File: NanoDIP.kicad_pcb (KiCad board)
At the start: 2 copper layers, 71.1 x 23.9 mm, 13 parts, among them SW1 SW_Push, U1 LM7805_TO220, U2 ATMEGA328P-PU, Y1 16 MHz

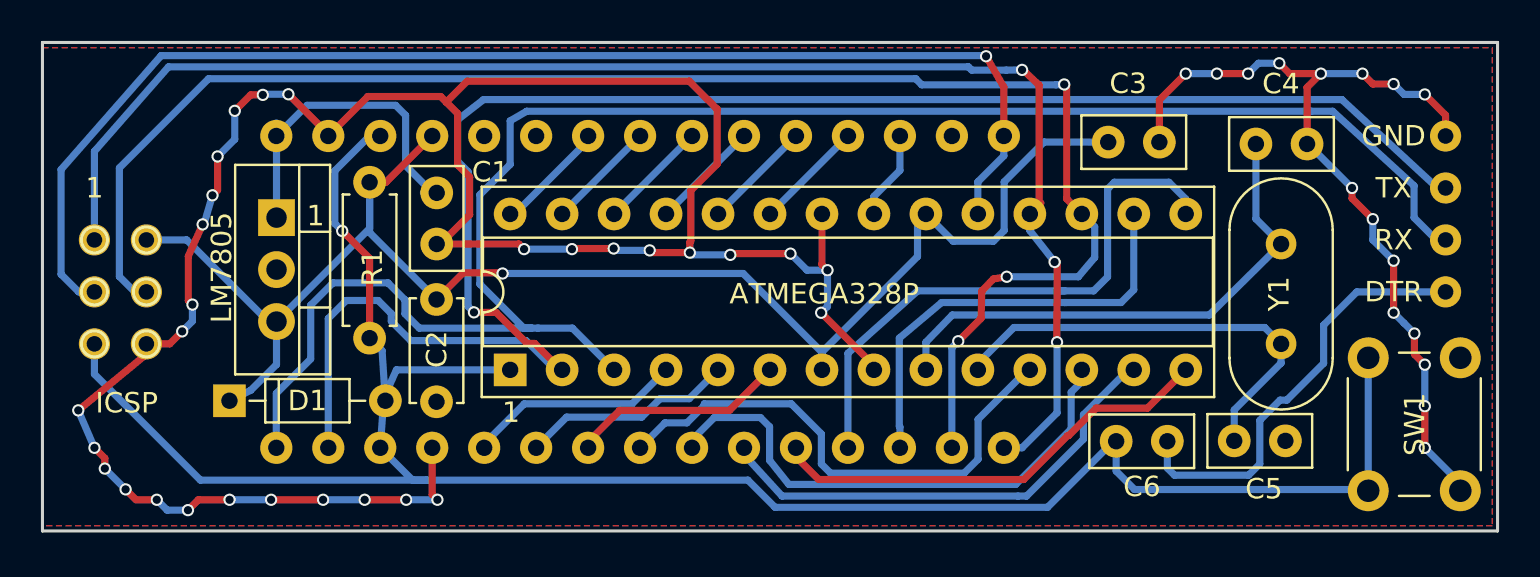
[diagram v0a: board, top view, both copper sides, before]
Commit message: Added pin labels
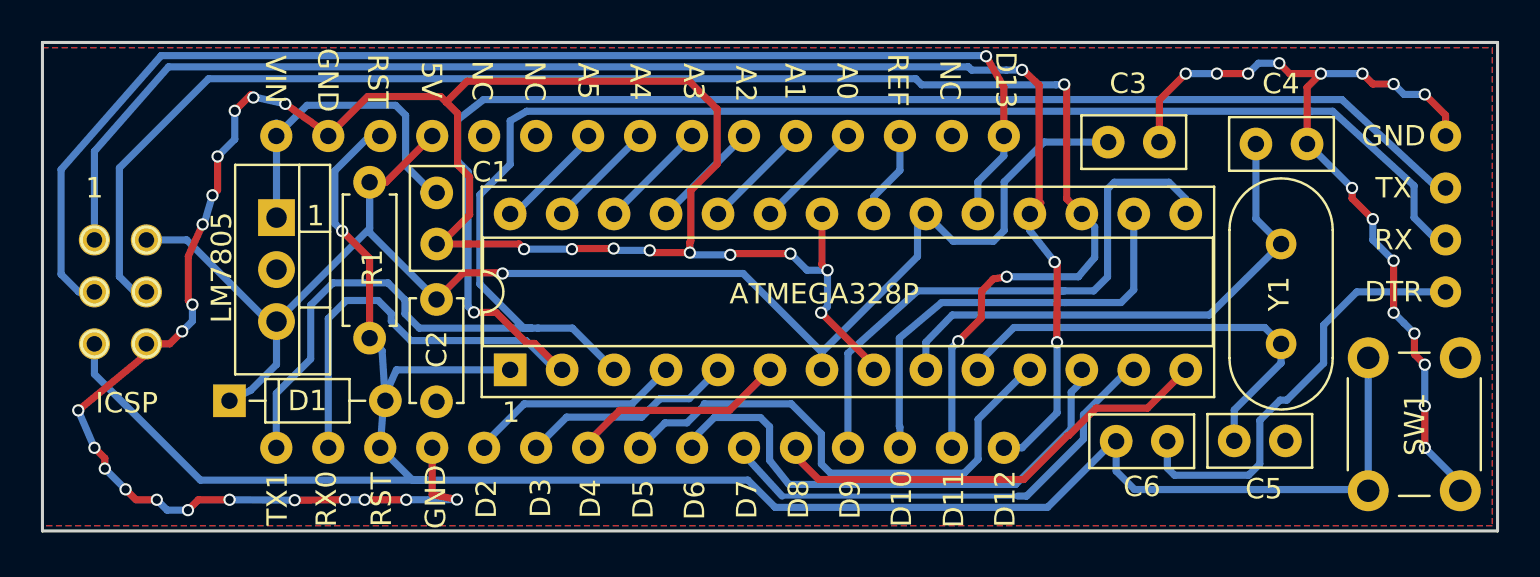
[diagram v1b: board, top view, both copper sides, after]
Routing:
- net GND: track 155.5 -> 157.1 mm
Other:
- board text added: "5V"
- board text added: "A0"
- board text added: "A1"
- board text added: "A2"
- board text added: "A3"
- board text added: "A4"
- board text added: "A5"
- board text added: "D10"
- board text added: "D11"
- board text added: "D12"
- board text added: "D13"
- board text added: "D2"
- board text added: "D3"
- board text added: "D4"
- board text added: "D5"
- board text added: "D6"
- board text added: "D7"
- board text added: "D8"
- board text added: "D9"
- board text added: "NC"
- board text added: "REF"
- board text added: "RST"
- board text added: "RX0"
- board text added: "TX1"
- board text added: "VIN"
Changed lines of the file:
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@@
     (links 62)
     (no_connects 0)
-    (area 121.844999 76.581999 193.115001 100.659001)
+    (area 121.844999 76.632999 193.115001 100.659001)
     (thickness 1.6)
-    (drawings 13)
+    (drawings 43)
     (tracks 443)
     (zones 0)
@@
   )
   (setup
-    (last_trace_width 0.35)
+    (last_trace_width 0.25)
     (user_trace_width 0.35)
     (trace_clearance 0.2)
@@
     (pad_to_mask_clearance 0.2)
     (aux_axis_origin 0 0)
-    (visible_elements FFFFFF7F)
+    (visible_elements 7FFFFFFF)
     (pcbplotparams
       (layerselection 0x00030_80000001)
@@
       (net 28 "Net-(A1-Pad40)"))
   )
+  (gr_text VIN (at 133.3 78.51 270) (layer F.SilkS)
+    (effects (font (size 1 1) (thickness 0.15)))
+  )
+  (gr_text GND (at 135.86 78.55 270) (layer F.SilkS)
+    (effects (font (size 1 1) (thickness 0.15)))
+  )
+  (gr_text RST (at 138.3 78.6 270) (layer F.SilkS)
+    (effects (font (size 1 1) (thickness 0.15)))
+  )
+  (gr_text 5V (at 140.93 78.54 270) (layer F.SilkS)
+    (effects (font (size 1 1) (thickness 0.15)))
+  )
+  (gr_text NC (at 143.4 78.57 270) (layer F.SilkS)
+    (effects (font (size 1 1) (thickness 0.15)))
+  )
+  (gr_text NC (at 145.98 78.6 270) (layer F.SilkS)
+    (effects (font (size 1 1) (thickness 0.15)))
+  )
+  (gr_text A5 (at 148.58 78.59 270) (layer F.SilkS)
+    (effects (font (size 1 1) (thickness 0.15)))
+  )
+  (gr_text A4 (at 151.12 78.64 270) (layer F.SilkS)
+    (effects (font (size 1 1) (thickness 0.15)))
+  )
+  (gr_text A3 (at 153.74 78.62 270) (layer F.SilkS)
+    (effects (font (size 1 1) (thickness 0.15)))
+  )
+  (gr_text A2 (at 156.29 78.73 270) (layer F.SilkS)
+    (effects (font (size 1 1) (thickness 0.15)))
+  )
+  (gr_text A1 (at 158.69 78.62 270) (layer F.SilkS)
+    (effects (font (size 1 1) (thickness 0.15)))
+  )
+  (gr_text A0 (at 161.24 78.61 270) (layer F.SilkS)
+    (effects (font (size 1 1) (thickness 0.15)))
+  )
+  (gr_text REF (at 163.72 78.55 270) (layer F.SilkS)
+    (effects (font (size 1 1) (thickness 0.15)))
+  )
+  (gr_text NC (at 166.27 78.55 270) (layer F.SilkS)
+    (effects (font (size 1 1) (thickness 0.15)))
+  )
+  (gr_text D13 (at 169 78.54 270) (layer F.SilkS)
+    (effects (font (size 1 1) (thickness 0.15)))
+  )
+  (gr_text D12 (at 168.97 99.01 90) (layer F.SilkS)
+    (effects (font (size 1 1) (thickness 0.15)))
+  )
+  (gr_text D11 (at 166.46 99.04 90) (layer F.SilkS)
+    (effects (font (size 1 1) (thickness 0.15)))
+  )
+  (gr_text D10 (at 163.91 99 90) (layer F.SilkS)
+    (effects (font (size 1 1) (thickness 0.15)))
+  )
+  (gr_text D9 (at 161.4 99.05 90) (layer F.SilkS)
+    (effects (font (size 1 1) (thickness 0.15)))
+  )
+  (gr_text D8 (at 158.88 99.04 90) (layer F.SilkS)
+    (effects (font (size 1 1) (thickness 0.15)))
+  )
+  (gr_text D7 (at 156.35 99.04 90) (layer F.SilkS)
+    (effects (font (size 1 1) (thickness 0.15)))
+  )
+  (gr_text D6 (at 153.8 99.09 90) (layer F.SilkS)
+    (effects (font (size 1 1) (thickness 0.15)))
+  )
+  (gr_text D5 (at 151.28 99.04 90) (layer F.SilkS)
+    (effects (font (size 1 1) (thickness 0.15)))
+  )
+  (gr_text D4 (at 148.71 99.01 90) (layer F.SilkS)
+    (effects (font (size 1 1) (thickness 0.15)))
+  )
+  (gr_text D3 (at 146.27 98.97 90) (layer F.SilkS)
+    (effects (font (size 1 1) (thickness 0.15)))
+  )
+  (gr_text D2 (at 143.62 99.02 90) (layer F.SilkS)
+    (effects (font (size 1 1) (thickness 0.15)))
+  )
+  (gr_text GND (at 141.14 98.92 90) (layer F.SilkS)
+    (effects (font (size 1 1) (thickness 0.15)))
+  )
+  (gr_text RX0 (at 135.8 99.02 90) (layer F.SilkS)
+    (effects (font (size 1 1) (thickness 0.15)))
+  )
+  (gr_text RST (at 138.49 99.05 90) (layer F.SilkS)
+    (effects (font (size 1 1) (thickness 0.15)))
+  )
+  (gr_text TX1 (at 133.4 99 90) (layer F.SilkS)
+    (effects (font (size 1 1) (thickness 0.15)))
+  )
   (gr_text LM7805 (at 130.68 87.71 90) (layer F.SilkS)
     (effects (font (size 1 1) (thickness 0.15)))
@@
   (segment (start 141.38 79.35) (end 137.82 79.35) (width 0.35) (layer F.Cu) (net 3))
   (segment (start 127 91.44) (end 128.14 91.44) (width 0.35) (layer F.Cu) (net 3))
-  (segment (start 133.94 79.24) (end 135.89 81.19) (width 0.35) (layer F.Cu) (net 3))
-  (via (at 133.94 79.24) (size 0.6) (drill 0.4) (layers F.Cu B.Cu) (net 3))
-  (segment (start 132.72 79.24) (end 133.94 79.24) (width 0.35) (layer B.Cu) (net 3))
-  (segment (start 132.69 79.27) (end 132.72 79.24) (width 0.35) (layer B.Cu) (net 3))
-  (via (at 132.69 79.27) (size 0.6) (drill 0.4) (layers F.Cu B.Cu) (net 3))
-  (segment (start 132.1 79.27) (end 132.69 79.27) (width 0.35) (layer F.Cu) (net 3))
+  (segment (start 133.79 79.71) (end 135.89 81.19) (width 0.35) (layer F.Cu) (net 3))
+  (via (at 133.79 79.71) (size 0.6) (drill 0.4) (layers F.Cu B.Cu) (net 3))
+  (segment (start 132.26 79.37) (end 133.79 79.71) (width 0.35) (layer B.Cu) (net 3))
+  (segment (start 132.23 79.4) (end 132.26 79.37) (width 0.35) (layer B.Cu) (net 3))
+  (via (at 132.23 79.4) (size 0.6) (drill 0.4) (layers F.Cu B.Cu) (net 3))
+  (segment (start 132.1 79.27) (end 132.23 79.4) (width 0.35) (layer F.Cu) (net 3))
   (segment (start 131.32 80.05) (end 132.1 79.27) (width 0.35) (layer F.Cu) (net 3))
   (via (at 131.32 80.05) (size 0.6) (drill 0.4) (layers F.Cu B.Cu) (net 3))
@@
   (segment (start 129.54 99.06) (end 131.064 99.06) (width 0.35) (layer F.Cu) (net 3))
   (via (at 131.064 99.06) (size 0.6) (drill 0.4) (layers F.Cu B.Cu) (net 3))
-  (segment (start 131.064 99.06) (end 133.096 99.06) (width 0.35) (layer B.Cu) (net 3))
-  (via (at 133.096 99.06) (size 0.6) (drill 0.4) (layers F.Cu B.Cu) (net 3))
-  (segment (start 133.096 99.06) (end 135.636 99.06) (width 0.35) (layer F.Cu) (net 3))
-  (via (at 135.636 99.06) (size 0.6) (drill 0.4) (layers F.Cu B.Cu) (net 3))
-  (segment (start 135.636 99.06) (end 137.668 99.06) (width 0.35) (layer B.Cu) (net 3))
+  (segment (start 131.064 99.06) (end 134.25 99.08) (width 0.35) (layer B.Cu) (net 3))
+  (via (at 134.25 99.08) (size 0.6) (drill 0.4) (layers F.Cu B.Cu) (net 3))
+  (segment (start 134.25 99.08) (end 136.7 99.06) (width 0.35) (layer F.Cu) (net 3))
+  (via (at 136.7 99.06) (size 0.6) (drill 0.4) (layers F.Cu B.Cu) (net 3))
+  (segment (start 136.7 99.06) (end 137.668 99.06) (width 0.35) (layer B.Cu) (net 3))
   (via (at 137.668 99.06) (size 0.6) (drill 0.4) (layers F.Cu B.Cu) (net 3))
   (segment (start 137.668 99.06) (end 139.7 99.06) (width 0.35) (layer F.Cu) (net 3))
   (via (at 139.7 99.06) (size 0.6) (drill 0.4) (layers F.Cu B.Cu) (net 3))
-  (segment (start 139.7 99.06) (end 141.224 99.06) (width 0.35) (layer B.Cu) (net 3))
-  (via (at 141.224 99.06) (size 0.6) (drill 0.4) (layers F.Cu B.Cu) (net 3))
-  (segment (start 141.224 99.06) (end 140.97 98.806) (width 0.35) (layer F.Cu) (net 3))
+  (segment (start 139.7 99.06) (end 142.18 99.05) (width 0.35) (layer B.Cu) (net 3))
+  (via (at 142.18 99.05) (size 0.6) (drill 0.4) (layers F.Cu B.Cu) (net 3))
+  (segment (start 142.18 99.05) (end 140.97 98.806) (width 0.35) (layer F.Cu) (net 3))
   (segment (start 140.97 98.806) (end 140.97 96.52) (width 0.35) (layer F.Cu) (net 3))
   (segment (start 190.5 83.82) (end 190.1 83.82) (width 0.35) (layer B.Cu) (net 4))
@@
   (segment (start 156.21 96.52) (end 156.21 96.85) (width 0.35) (layer B.Cu) (net 17))
   (segment (start 156.21 96.85) (end 158.07 98.88) (width 0.35) (layer B.Cu) (net 17))
-  (segment (start 158.07 98.88) (end 169.6 98.88) (width 0.35) (layer B.Cu) (net 17))
+  (segment (start 158.07 98.88) (end 169.6 98.88) (width 0.25) (layer B.Cu) (net 17))
   (segment (start 154.94 85.09) (end 158.75 81.28) (width 0.35) (layer B.Cu) (net 18) (status 10))
   (segment (start 158.75 96.52) (end 158.75 96.96) (width 0.35) (layer F.Cu) (net 19))
